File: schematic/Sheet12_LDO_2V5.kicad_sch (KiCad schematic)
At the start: 10 parts, among them U10 TPS7H1121-SP

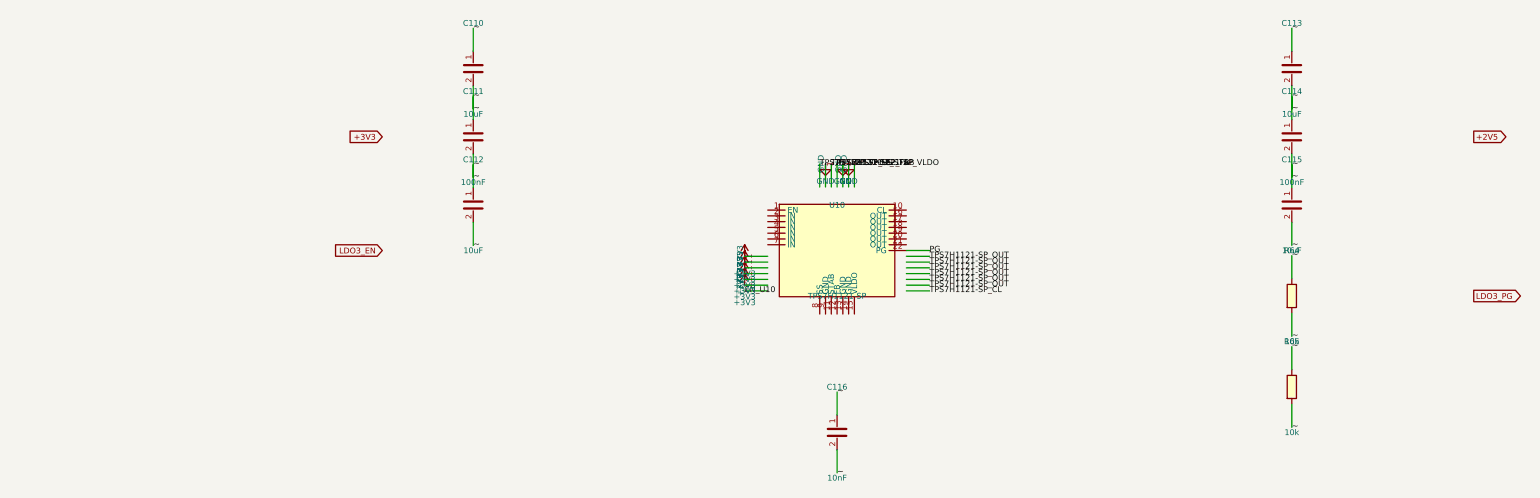
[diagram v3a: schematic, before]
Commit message: Fix KiCad schematic wiring: Y-inversion bug + all 891 pins connected
- Fixed critical Y-axis inversion bug: KiCad inverts Y when placing
  symbols (lib Y + schematic Y = abs Y is WRONG; correct: abs Y = sym Y - lib Y)
- This caused ALL wires to connect to wrong pins (e.g., CS label connected
  to BG pin instead of CS pin)
- Verified with netlist: 0 unconnected nets, all pin functions correct
- Fixed wire direction for angle 90/270 (swapped due to Y-inversion)
- 891 pin connections across 15 sheets, all 17 sheets export without errors
- Netlist verification: CS→E8, BG→C3, INA+→A4, CLK+→F1, JESD pairs correct

Co-Authored-By: opencode <noreply@opencode.ai>
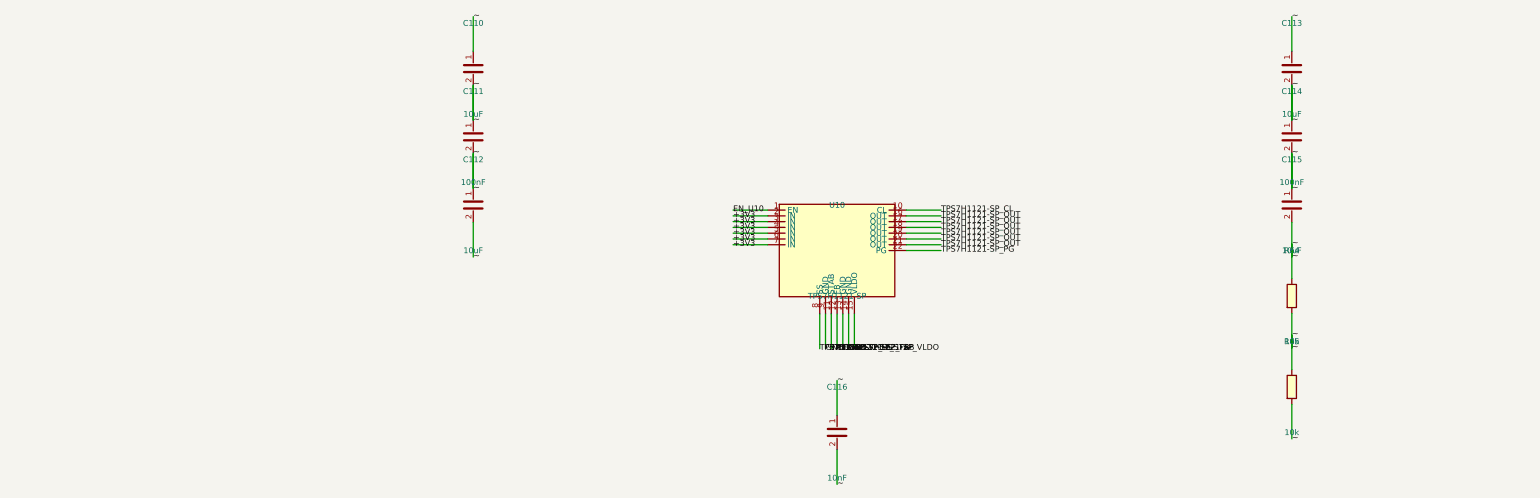
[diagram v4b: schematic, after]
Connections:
- net +3V3: now also U10.2 (IN), U10.3 (IN), U10.4 (IN), U10.5 (IN), U10.6 (IN), U10.7 (IN)
- net EN_U10: now also U10.1 (EN)
- net GND: now also U10.13 (GND), U10.14 (GND), U10.9 (GND)
- net TPS7H1121-SP_CL: now also U10.10 (CL)
- net TPS7H1121-SP_FB: now also U10.12 (FB)
- net TPS7H1121-SP_OUT: now also U10.16 (OUT), U10.17 (OUT), U10.18 (OUT), U10.19 (OUT), U10.20 (OUT), U10.21 (OUT)
- net TPS7H1121-SP_SS: now also U10.8 (SS)
- net TPS7H1121-SP_STAB: now also U10.11 (STAB)
- net TPS7H1121-SP_VLDO: now also U10.15 (VLDO)
- net PG renamed TPS7H1121-SP_PG

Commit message: fix: replace wire stubs with labels-only to prevent power net shorts
Labels placed directly at pin endpoints eliminate wire overlap that
caused BGA power pins (VA11, VA19, VD11, AGND, DGND) to merge into
a single net. Verified via netlist: GND=52, +1V0_ANA=12, +1V9_ANA=12,
+1V1_DIG=10 nodes (all correct per datasheet pin mapping).
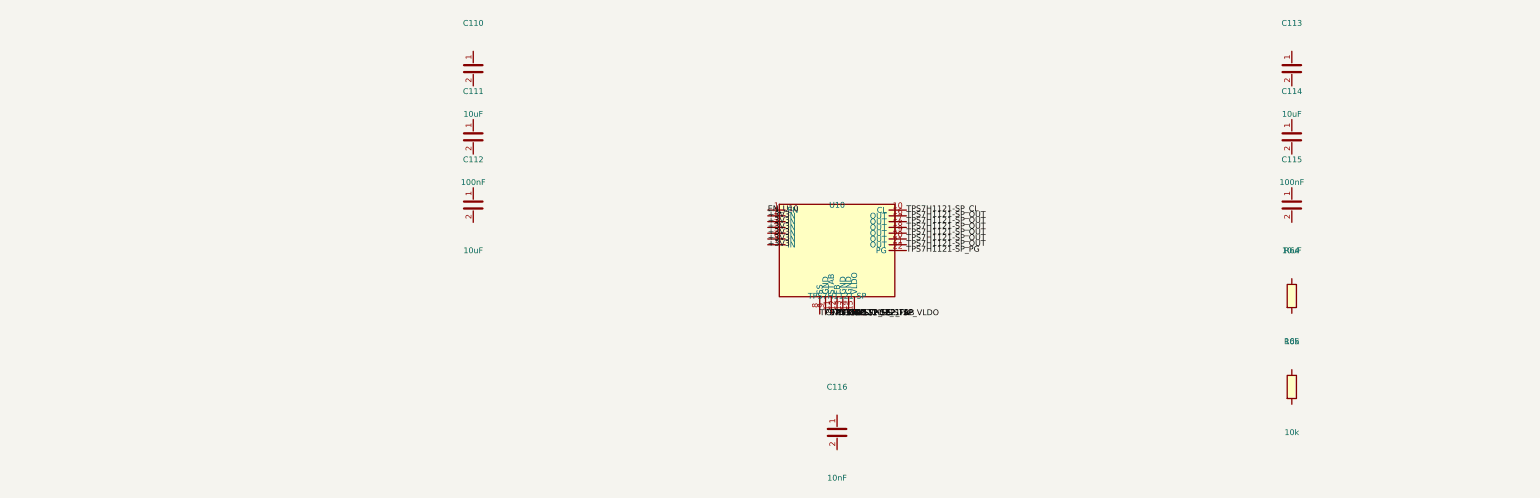
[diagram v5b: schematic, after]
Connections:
- removed net ~: C110.1, C110.2, C111.1, C111.2, C112.1, C112.2, C113.1, C113.2, C114.1, C114.2, C115.1, C115.2, C116.1, C116.2, R64.1, R64.2, R65.1, R65.2
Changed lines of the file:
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@@
     (pin "2")
   )
-  (wire (pts (xy 184.7600 71.1100) (xy 177.1400 71.1100)) (stroke (width 0) (type default)))
-  (label "EN_U10" (at 177.1400 71.1100 0) (effects (font (size 1.27 1.27))))
-  (wire (pts (xy 184.7600 72.3800) (xy 177.1400 72.3800)) (stroke (width 0) (type default)))
-  (label "+3V3" (at 177.1400 72.3800 0) (effects (font (size 1.27 1.27))))
-  (wire (pts (xy 184.7600 73.6500) (xy 177.1400 73.6500)) (stroke (width 0) (type default)))
-  (label "+3V3" (at 177.1400 73.6500 0) (effects (font (size 1.27 1.27))))
-  (wire (pts (xy 184.7600 74.9200) (xy 177.1400 74.9200)) (stroke (width 0) (type default)))
-  (label "+3V3" (at 177.1400 74.9200 0) (effects (font (size 1.27 1.27))))
-  (wire (pts (xy 184.7600 76.1900) (xy 177.1400 76.1900)) (stroke (width 0) (type default)))
-  (label "+3V3" (at 177.1400 76.1900 0) (effects (font (size 1.27 1.27))))
-  (wire (pts (xy 184.7600 77.4600) (xy 177.1400 77.4600)) (stroke (width 0) (type default)))
-  (label "+3V3" (at 177.1400 77.4600 0) (effects (font (size 1.27 1.27))))
-  (wire (pts (xy 184.7600 78.7300) (xy 177.1400 78.7300)) (stroke (width 0) (type default)))
-  (label "+3V3" (at 177.1400 78.7300 0) (effects (font (size 1.27 1.27))))
-  (wire (pts (xy 215.2400 71.1100) (xy 222.8600 71.1100)) (stroke (width 0) (type default)))
-  (label "TPS7H1121-SP_CL" (at 222.8600 71.1100 0) (effects (font (size 1.27 1.27))))
-  (wire (pts (xy 215.2400 72.3800) (xy 222.8600 72.3800)) (stroke (width 0) (type default)))
-  (label "TPS7H1121-SP_OUT" (at 222.8600 72.3800 0) (effects (font (size 1.27 1.27))))
-  (wire (pts (xy 215.2400 73.6500) (xy 222.8600 73.6500)) (stroke (width 0) (type default)))
-  (label "TPS7H1121-SP_OUT" (at 222.8600 73.6500 0) (effects (font (size 1.27 1.27))))
-  (wire (pts (xy 215.2400 74.9200) (xy 222.8600 74.9200)) (stroke (width 0) (type default)))
-  (label "TPS7H1121-SP_OUT" (at 222.8600 74.9200 0) (effects (font (size 1.27 1.27))))
-  (wire (pts (xy 215.2400 76.1900) (xy 222.8600 76.1900)) (stroke (width 0) (type default)))
-  (label "TPS7H1121-SP_OUT" (at 222.8600 76.1900 0) (effects (font (size 1.27 1.27))))
-  (wire (pts (xy 215.2400 77.4600) (xy 222.8600 77.4600)) (stroke (width 0) (type default)))
-  (label "TPS7H1121-SP_OUT" (at 222.8600 77.4600 0) (effects (font (size 1.27 1.27))))
-  (wire (pts (xy 215.2400 78.7300) (xy 222.8600 78.7300)) (stroke (width 0) (type default)))
-  (label "TPS7H1121-SP_OUT" (at 222.8600 78.7300 0) (effects (font (size 1.27 1.27))))
-  (wire (pts (xy 215.2400 80.0000) (xy 222.8600 80.0000)) (stroke (width 0) (type default)))
-  (label "TPS7H1121-SP_PG" (at 222.8600 80.0000 0) (effects (font (size 1.27 1.27))))
-  (wire (pts (xy 196.1900 93.9700) (xy 196.1900 101.5900)) (stroke (width 0) (type default)))
-  (label "TPS7H1121-SP_SS" (at 196.1900 101.5900 0) (effects (font (size 1.27 1.27))))
-  (wire (pts (xy 197.4600 93.9700) (xy 197.4600 101.5900)) (stroke (width 0) (type default)))
-  (label "GND" (at 197.4600 101.5900 0) (effects (font (size 1.27 1.27))))
-  (wire (pts (xy 198.7300 93.9700) (xy 198.7300 101.5900)) (stroke (width 0) (type default)))
-  (label "TPS7H1121-SP_STAB" (at 198.7300 101.5900 0) (effects (font (size 1.27 1.27))))
-  (wire (pts (xy 200.0000 93.9700) (xy 200.0000 101.5900)) (stroke (width 0) (type default)))
-  (label "TPS7H1121-SP_FB" (at 200.0000 101.5900 0) (effects (font (size 1.27 1.27))))
-  (wire (pts (xy 201.2700 93.9700) (xy 201.2700 101.5900)) (stroke (width 0) (type default)))
-  (label "GND" (at 201.2700 101.5900 0) (effects (font (size 1.27 1.27))))
-  (wire (pts (xy 202.5400 93.9700) (xy 202.5400 101.5900)) (stroke (width 0) (type default)))
-  (label "GND" (at 202.5400 101.5900 0) (effects (font (size 1.27 1.27))))
-  (wire (pts (xy 203.8100 93.9700) (xy 203.8100 101.5900)) (stroke (width 0) (type default)))
-  (label "TPS7H1121-SP_VLDO" (at 203.8100 101.5900 0) (effects (font (size 1.27 1.27))))
-  (wire (pts (xy 120.0000 36.1900) (xy 120.0000 28.5700)) (stroke (width 0) (type default)))
-  (label "~" (at 120.0000 28.5700 0) (effects (font (size 1.27 1.27))))
-  (wire (pts (xy 120.0000 43.8100) (xy 120.0000 51.4300)) (stroke (width 0) (type default)))
-  (label "~" (at 120.0000 51.4300 0) (effects (font (size 1.27 1.27))))
-  (wire (pts (xy 120.0000 51.1900) (xy 120.0000 43.5700)) (stroke (width 0) (type default)))
-  (label "~" (at 120.0000 43.5700 0) (effects (font (size 1.27 1.27))))
-  (wire (pts (xy 120.0000 58.8100) (xy 120.0000 66.4300)) (stroke (width 0) (type default)))
-  (label "~" (at 120.0000 66.4300 0) (effects (font (size 1.27 1.27))))
-  (wire (pts (xy 120.0000 66.1900) (xy 120.0000 58.5700)) (stroke (width 0) (type default)))
-  (label "~" (at 120.0000 58.5700 0) (effects (font (size 1.27 1.27))))
-  (wire (pts (xy 120.0000 73.8100) (xy 120.0000 81.4300)) (stroke (width 0) (type default)))
-  (label "~" (at 120.0000 81.4300 0) (effects (font (size 1.27 1.27))))
-  (wire (pts (xy 300.0000 36.1900) (xy 300.0000 28.5700)) (stroke (width 0) (type default)))
-  (label "~" (at 300.0000 28.5700 0) (effects (font (size 1.27 1.27))))
-  (wire (pts (xy 300.0000 43.8100) (xy 300.0000 51.4300)) (stroke (width 0) (type default)))
-  (label "~" (at 300.0000 51.4300 0) (effects (font (size 1.27 1.27))))
-  (wire (pts (xy 300.0000 51.1900) (xy 300.0000 43.5700)) (stroke (width 0) (type default)))
-  (label "~" (at 300.0000 43.5700 0) (effects (font (size 1.27 1.27))))
-  (wire (pts (xy 300.0000 58.8100) (xy 300.0000 66.4300)) (stroke (width 0) (type default)))
-  (label "~" (at 300.0000 66.4300 0) (effects (font (size 1.27 1.27))))
-  (wire (pts (xy 300.0000 66.1900) (xy 300.0000 58.5700)) (stroke (width 0) (type default)))
-  (label "~" (at 300.0000 58.5700 0) (effects (font (size 1.27 1.27))))
-  (wire (pts (xy 300.0000 73.8100) (xy 300.0000 81.4300)) (stroke (width 0) (type default)))
-  (label "~" (at 300.0000 81.4300 0) (effects (font (size 1.27 1.27))))
-  (wire (pts (xy 200.0000 116.1900) (xy 200.0000 108.5700)) (stroke (width 0) (type default)))
-  (label "~" (at 200.0000 108.5700 0) (effects (font (size 1.27 1.27))))
-  (wire (pts (xy 200.0000 123.8100) (xy 200.0000 131.4300)) (stroke (width 0) (type default)))
-  (label "~" (at 200.0000 131.4300 0) (effects (font (size 1.27 1.27))))
-  (wire (pts (xy 300.0000 86.1900) (xy 300.0000 78.5700)) (stroke (width 0) (type default)))
-  (label "~" (at 300.0000 78.5700 0) (effects (font (size 1.27 1.27))))
-  (wire (pts (xy 300.0000 93.8100) (xy 300.0000 101.4300)) (stroke (width 0) (type default)))
-  (label "~" (at 300.0000 101.4300 0) (effects (font (size 1.27 1.27))))
-  (wire (pts (xy 300.0000 106.1900) (xy 300.0000 98.5700)) (stroke (width 0) (type default)))
-  (label "~" (at 300.0000 98.5700 0) (effects (font (size 1.27 1.27))))
-  (wire (pts (xy 300.0000 113.8100) (xy 300.0000 121.4300)) (stroke (width 0) (type default)))
-  (label "~" (at 300.0000 121.4300 0) (effects (font (size 1.27 1.27))))
+  (label "EN_U10" (at 184.7600 71.1100 0) (effects (font (size 1.27 1.27))))
+  (label "+3V3" (at 184.7600 72.3800 0) (effects (font (size 1.27 1.27))))
+  (label "+3V3" (at 184.7600 73.6500 0) (effects (font (size 1.27 1.27))))
+  (label "+3V3" (at 184.7600 74.9200 0) (effects (font (size 1.27 1.27))))
+  (label "+3V3" (at 184.7600 76.1900 0) (effects (font (size 1.27 1.27))))
+  (label "+3V3" (at 184.7600 77.4600 0) (effects (font (size 1.27 1.27))))
+  (label "+3V3" (at 184.7600 78.7300 0) (effects (font (size 1.27 1.27))))
+  (label "TPS7H1121-SP_CL" (at 215.2400 71.1100 0) (effects (font (size 1.27 1.27))))
+  (label "TPS7H1121-SP_OUT" (at 215.2400 72.3800 0) (effects (font (size 1.27 1.27))))
+  (label "TPS7H1121-SP_OUT" (at 215.2400 73.6500 0) (effects (font (size 1.27 1.27))))
+  (label "TPS7H1121-SP_OUT" (at 215.2400 74.9200 0) (effects (font (size 1.27 1.27))))
+  (label "TPS7H1121-SP_OUT" (at 215.2400 76.1900 0) (effects (font (size 1.27 1.27))))
+  (label "TPS7H1121-SP_OUT" (at 215.2400 77.4600 0) (effects (font (size 1.27 1.27))))
+  (label "TPS7H1121-SP_OUT" (at 215.2400 78.7300 0) (effects (font (size 1.27 1.27))))
+  (label "TPS7H1121-SP_PG" (at 215.2400 80.0000 0) (effects (font (size 1.27 1.27))))
+  (label "TPS7H1121-SP_SS" (at 196.1900 93.9700 0) (effects (font (size 1.27 1.27))))
+  (label "GND" (at 197.4600 93.9700 0) (effects (font (size 1.27 1.27))))
+  (label "TPS7H1121-SP_STAB" (at 198.7300 93.9700 0) (effects (font (size 1.27 1.27))))
+  (label "TPS7H1121-SP_FB" (at 200.0000 93.9700 0) (effects (font (size 1.27 1.27))))
+  (label "GND" (at 201.2700 93.9700 0) (effects (font (size 1.27 1.27))))
+  (label "GND" (at 202.5400 93.9700 0) (effects (font (size 1.27 1.27))))
+  (label "TPS7H1121-SP_VLDO" (at 203.8100 93.9700 0) (effects (font (size 1.27 1.27))))
   (sheet_instances (path "/" (page "1")))
 )

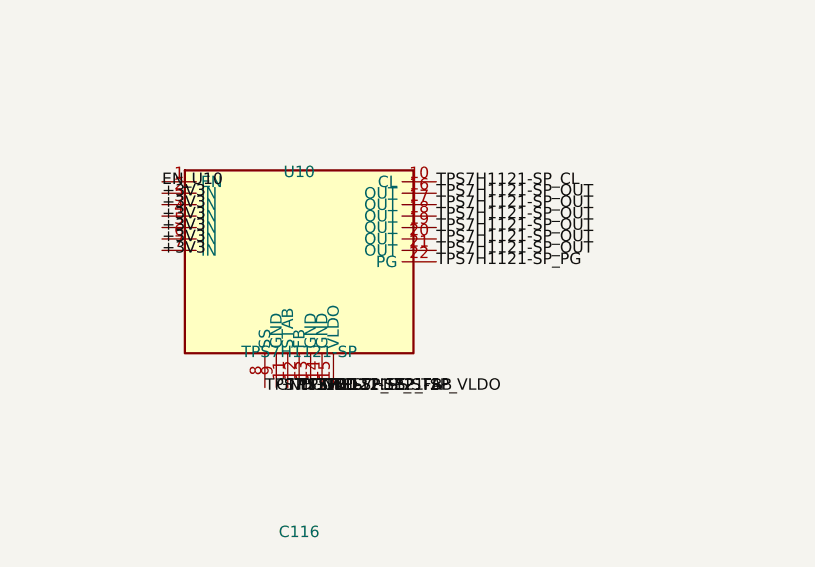
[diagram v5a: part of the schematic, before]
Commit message: fix: isolate ISL70003ASEH buck pins, fix LMX_SYNC collision, NC pins, connector pin names
- ISL70003ASEH pins now use ref prefix (U6_LX1 vs U7_LX1) to prevent shorts
- Buck SYNC pins separated from LMX_SYNC (power sync ≠ PLL sync)
- NC pins properly skipped (unconnected)
- Connector PIN_1..PIN_6 use ref prefix (J1_PIN_1 vs J2_PIN_1)
- Fixed annotation warnings in Sheet13 (C_dev→C125, R_dev→R74, U_TPS7H→U14)
- Regenerated all PDFs and SVGs
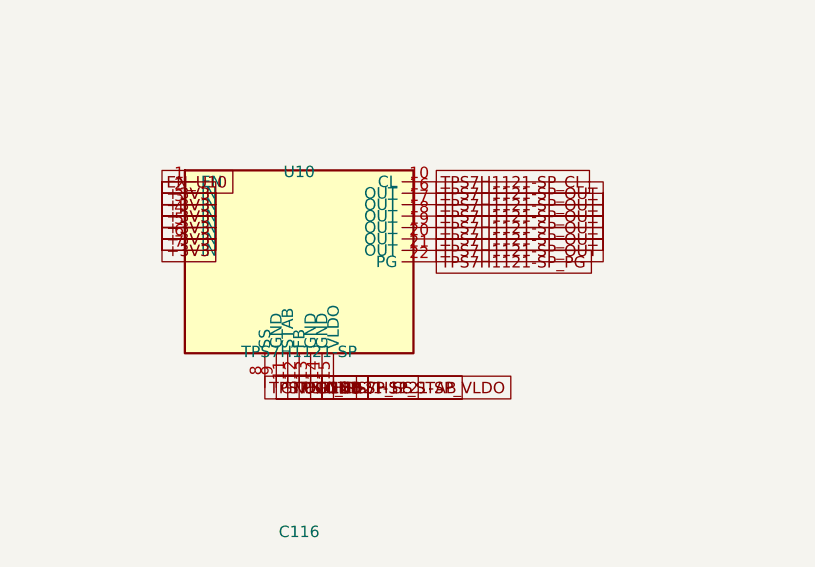
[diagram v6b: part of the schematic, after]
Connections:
- net TPS7H1121-SP_FB renamed U10_FB
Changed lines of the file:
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@@
     (pin "2")
   )
-  (label "EN_U10" (at 184.7600 71.1100 0) (effects (font (size 1.27 1.27))))
-  (label "+3V3" (at 184.7600 72.3800 0) (effects (font (size 1.27 1.27))))
-  (label "+3V3" (at 184.7600 73.6500 0) (effects (font (size 1.27 1.27))))
-  (label "+3V3" (at 184.7600 74.9200 0) (effects (font (size 1.27 1.27))))
-  (label "+3V3" (at 184.7600 76.1900 0) (effects (font (size 1.27 1.27))))
-  (label "+3V3" (at 184.7600 77.4600 0) (effects (font (size 1.27 1.27))))
-  (label "+3V3" (at 184.7600 78.7300 0) (effects (font (size 1.27 1.27))))
-  (label "TPS7H1121-SP_CL" (at 215.2400 71.1100 0) (effects (font (size 1.27 1.27))))
-  (label "TPS7H1121-SP_OUT" (at 215.2400 72.3800 0) (effects (font (size 1.27 1.27))))
-  (label "TPS7H1121-SP_OUT" (at 215.2400 73.6500 0) (effects (font (size 1.27 1.27))))
-  (label "TPS7H1121-SP_OUT" (at 215.2400 74.9200 0) (effects (font (size 1.27 1.27))))
-  (label "TPS7H1121-SP_OUT" (at 215.2400 76.1900 0) (effects (font (size 1.27 1.27))))
-  (label "TPS7H1121-SP_OUT" (at 215.2400 77.4600 0) (effects (font (size 1.27 1.27))))
-  (label "TPS7H1121-SP_OUT" (at 215.2400 78.7300 0) (effects (font (size 1.27 1.27))))
-  (label "TPS7H1121-SP_PG" (at 215.2400 80.0000 0) (effects (font (size 1.27 1.27))))
-  (label "TPS7H1121-SP_SS" (at 196.1900 93.9700 0) (effects (font (size 1.27 1.27))))
-  (label "GND" (at 197.4600 93.9700 0) (effects (font (size 1.27 1.27))))
-  (label "TPS7H1121-SP_STAB" (at 198.7300 93.9700 0) (effects (font (size 1.27 1.27))))
-  (label "TPS7H1121-SP_FB" (at 200.0000 93.9700 0) (effects (font (size 1.27 1.27))))
-  (label "GND" (at 201.2700 93.9700 0) (effects (font (size 1.27 1.27))))
-  (label "GND" (at 202.5400 93.9700 0) (effects (font (size 1.27 1.27))))
-  (label "TPS7H1121-SP_VLDO" (at 203.8100 93.9700 0) (effects (font (size 1.27 1.27))))
+  (global_label "EN_U10" (at 184.7600 71.1100 0) (effects (font (size 1.27 1.27))))
+  (global_label "+3V3" (at 184.7600 72.3800 0) (effects (font (size 1.27 1.27))))
+  (global_label "+3V3" (at 184.7600 73.6500 0) (effects (font (size 1.27 1.27))))
+  (global_label "+3V3" (at 184.7600 74.9200 0) (effects (font (size 1.27 1.27))))
+  (global_label "+3V3" (at 184.7600 76.1900 0) (effects (font (size 1.27 1.27))))
+  (global_label "+3V3" (at 184.7600 77.4600 0) (effects (font (size 1.27 1.27))))
+  (global_label "+3V3" (at 184.7600 78.7300 0) (effects (font (size 1.27 1.27))))
+  (global_label "TPS7H1121-SP_CL" (at 215.2400 71.1100 0) (effects (font (size 1.27 1.27))))
+  (global_label "TPS7H1121-SP_OUT" (at 215.2400 72.3800 0) (effects (font (size 1.27 1.27))))
+  (global_label "TPS7H1121-SP_OUT" (at 215.2400 73.6500 0) (effects (font (size 1.27 1.27))))
+  (global_label "TPS7H1121-SP_OUT" (at 215.2400 74.9200 0) (effects (font (size 1.27 1.27))))
+  (global_label "TPS7H1121-SP_OUT" (at 215.2400 76.1900 0) (effects (font (size 1.27 1.27))))
+  (global_label "TPS7H1121-SP_OUT" (at 215.2400 77.4600 0) (effects (font (size 1.27 1.27))))
+  (global_label "TPS7H1121-SP_OUT" (at 215.2400 78.7300 0) (effects (font (size 1.27 1.27))))
+  (global_label "TPS7H1121-SP_PG" (at 215.2400 80.0000 0) (effects (font (size 1.27 1.27))))
+  (global_label "TPS7H1121-SP_SS" (at 196.1900 93.9700 0) (effects (font (size 1.27 1.27))))
+  (global_label "GND" (at 197.4600 93.9700 0) (effects (font (size 1.27 1.27))))
+  (global_label "TPS7H1121-SP_STAB" (at 198.7300 93.9700 0) (effects (font (size 1.27 1.27))))
+  (global_label "U10_FB" (at 200.0000 93.9700 0) (effects (font (size 1.27 1.27))))
+  (global_label "GND" (at 201.2700 93.9700 0) (effects (font (size 1.27 1.27))))
+  (global_label "GND" (at 202.5400 93.9700 0) (effects (font (size 1.27 1.27))))
+  (global_label "TPS7H1121-SP_VLDO" (at 203.8100 93.9700 0) (effects (font (size 1.27 1.27))))
   (sheet_instances (path "/" (page "1")))
 )
